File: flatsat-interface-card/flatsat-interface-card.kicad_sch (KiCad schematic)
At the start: 1 part, among them U1 MCP2221AxST

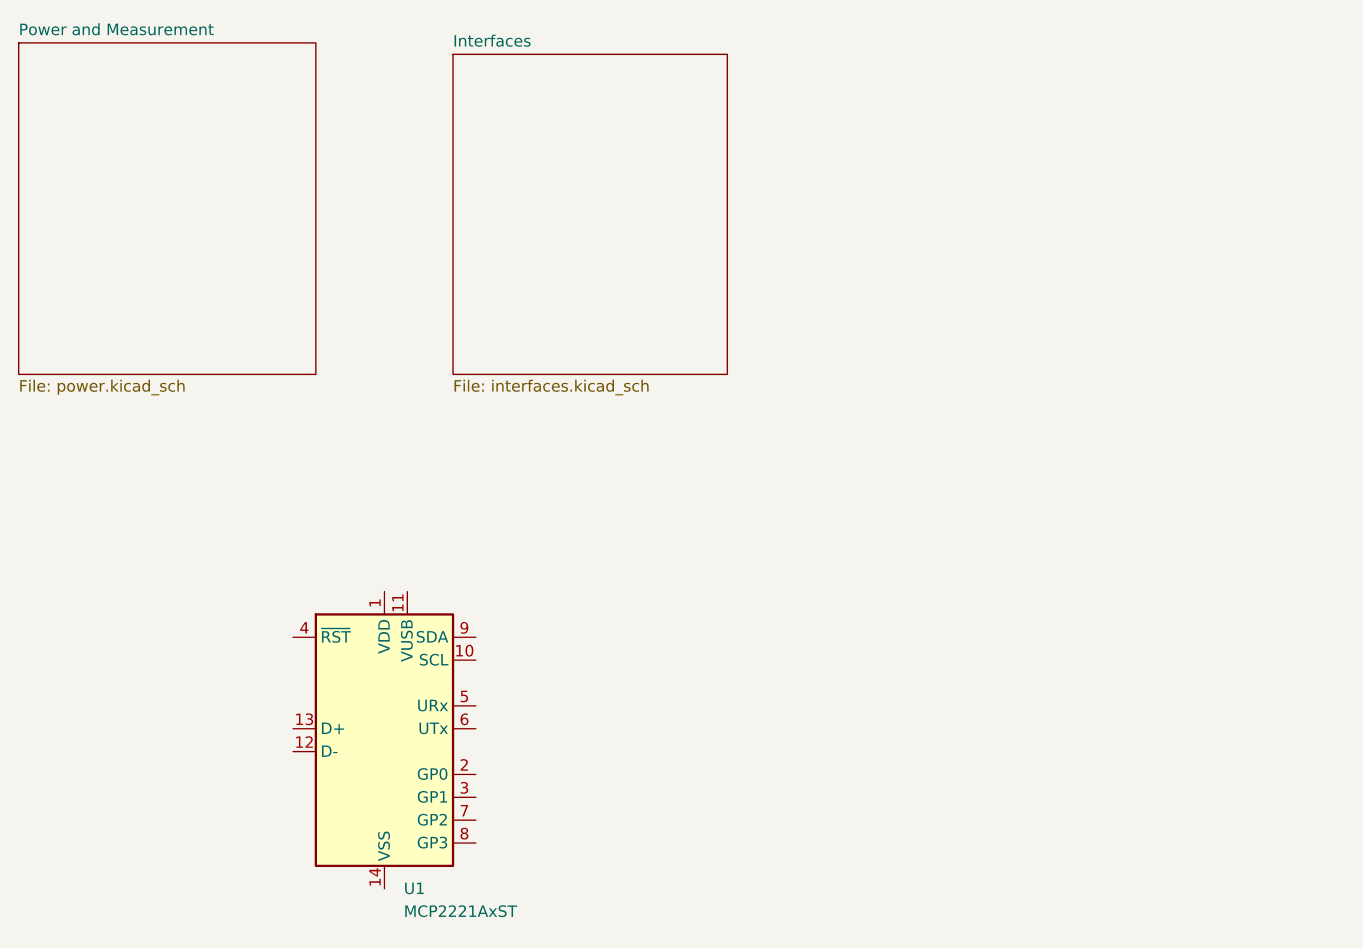
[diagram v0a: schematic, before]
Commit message: added new pages, identified i2c domain solution
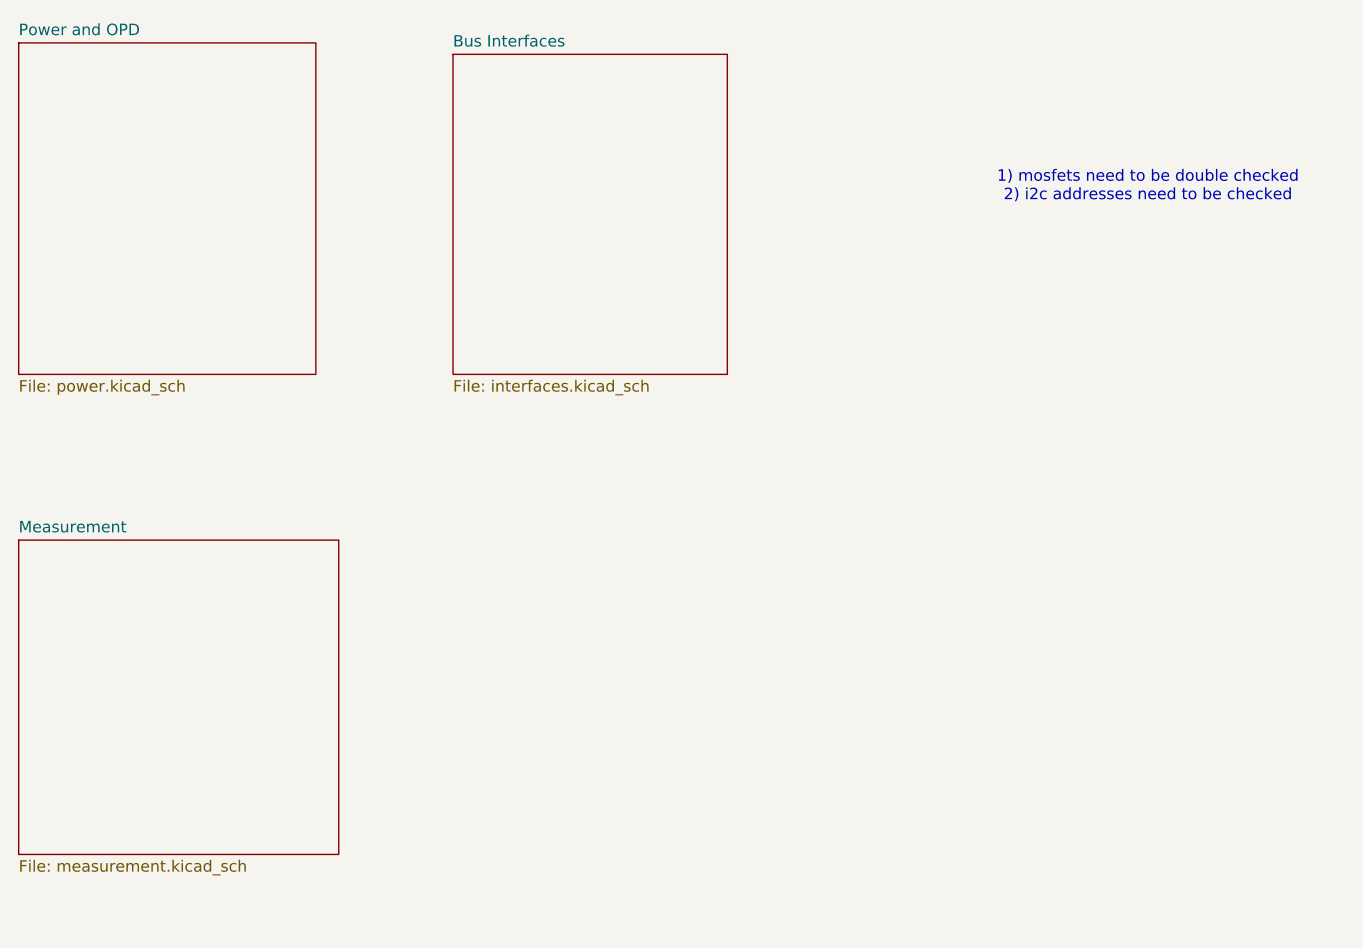
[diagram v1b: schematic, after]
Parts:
- removed U1: MCP2221AxST, Package_SO:TSSOP-14_4.4x5mm_P0.65mm, symbol Interface_USB:MCP2221AxST
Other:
- sheet Interfaces renamed Bus Interfaces
- sheet Power and Measurement renamed Power and OPD
- added sheet Measurement (measurement.kicad_sch)
- note added: "1) mosfets need to be double checked 2) i2c addresses need to be checked"
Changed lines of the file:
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@@
 	(title_block
 		(title "Flatsat Interface Card")
+		(date "2026-06-29")
 		(rev "0")
 		(company "Portland State Aerospace Society")
 	)
+	(text "1) mosfets need to be double checked\n2) i2c addresses need to be checked"
+		(exclude_from_sim no)
+		(at 221.996 54.102 0)
+		(effects
+			(font
+				(size 1.27 1.27)
+			)
+		)
+	)
 	(image
 		(at 257.81 173.99)
@@
 		)
 	)
-	(symbol
-		(lib_id "Interface_USB:MCP2221AxST")
-		(at 137.16 116.84 0)
-		(unit 1)
-		(body_style 1)
+	(sheet
+		(at 144.78 39.37)
+		(size 30.48 35.56)
 		(exclude_from_sim no)
 		(in_bom yes)
 		(on_board yes)
-		(in_pos_files yes)
 		(dnp no)
 		(fields_autoplaced yes)
-		(property "Reference" "U1"
-			(at 139.3033 132.08 0)
-			(show_name no)
-			(do_not_autoplace no)
-			(effects
-				(font
-					(size 1.27 1.27)
-				)
-				(justify left)
-			)
-		)
-		(property "Value" "MCP2221AxST"
-			(at 139.3033 134.62 0)
-			(show_name no)
-			(do_not_autoplace no)
-			(effects
-				(font
-					(size 1.27 1.27)
-				)
-				(justify left)
-			)
+		(stroke
+			(width 0.1524)
+			(type solid)
 		)
-		(property "Footprint" "Package_SO:TSSOP-14_4.4x5mm_P0.65mm"
-			(at 137.16 91.44 0)
-			(hide yes)
-			(show_name no)
-			(do_not_autoplace no)
-			(effects
-				(font
-					(size 1.27 1.27)
-				)
-			)
+		(fill
+			(color 0 0 0 0)
 		)
-		(property "Datasheet" "http://ww1.microchip.com/downloads/en/DeviceDoc/20005565B.pdf"
-			(at 137.16 99.06 0)
-			(hide yes)
+		(property "Sheetname" "Bus Interfaces"
+			(at 144.78 38.6584 0)
 			(show_name no)
 			(do_not_autoplace no)
@@
 					(size 1.27 1.27)
 				)
+				(justify left bottom)
 			)
 		)
-		(property "Description" "USB to I2C/UART Protocol Converter with GPIO, TSSOP-14"
-			(at 137.16 116.84 0)
-			(hide yes)
+		(property "Sheetfile" "interfaces.kicad_sch"
+			(at 144.78 75.5146 0)
 			(show_name no)
 			(do_not_autoplace no)
@@
 					(size 1.27 1.27)
 				)
+				(justify left top)
 			)
 		)
-		(pin "6"
-		)
-		(pin "2"
-		)
-		(pin "1"
-		)
-		(pin "4"
-		)
-		(pin "3"
-		)
-		(pin "5"
-		)
-		(pin "7"
-		)
-		(pin "11"
-		)
-		(pin "10"
-		)
-		(pin "9"
-		)
-		(pin "8"
-		)
-		(pin "14"
-		)
-		(pin "13"
-		)
-		(pin "12"
-		)
 		(instances
 			(project "flatsat-interface-card"
 				(path "/1a9202c4-e698-4c93-952c-ee3e64e9e49c"
-					(reference "U1")
-					(unit 1)
+					(page "3")
 				)
 			)
@@
 	)
 	(sheet
-		(at 144.78 39.37)
-		(size 30.48 35.56)
+		(at 96.52 38.1)
+		(size 33.02 36.83)
 		(exclude_from_sim no)
 		(in_bom yes)
@@
 			(color 0 0 0 0)
 		)
-		(property "Sheetname" "Interfaces"
-			(at 144.78 38.6584 0)
+		(property "Sheetname" "Power and OPD"
+			(at 96.52 37.3884 0)
 			(show_name no)
 			(do_not_autoplace no)
@@
 			)
 		)
-		(property "Sheetfile" "interfaces.kicad_sch"
-			(at 144.78 75.5146 0)
+		(property "Sheetfile" "power.kicad_sch"
+			(at 96.52 75.5146 0)
 			(show_name no)
 			(do_not_autoplace no)
@@
 			)
 		)
+		(property "Field2" ""
+			(at 96.52 38.1 0)
+			(hide yes)
+			(show_name no)
+			(do_not_autoplace no)
+			(effects
+				(font
+					(size 1.27 1.27)
+				)
+			)
+		)
 		(instances
 			(project "flatsat-interface-card"
 				(path "/1a9202c4-e698-4c93-952c-ee3e64e9e49c"
-					(page "3")
+					(page "2")
 				)
 			)
@@
 	)
 	(sheet
-		(at 96.52 38.1)
-		(size 33.02 36.83)
+		(at 96.52 93.345)
+		(size 35.56 34.925)
 		(exclude_from_sim no)
 		(in_bom yes)
@@
 			(color 0 0 0 0)
 		)
-		(property "Sheetname" "Power and Measurement"
-			(at 96.52 37.3884 0)
+		(property "Sheetname" "Measurement"
+			(at 96.52 92.6334 0)
 			(show_name no)
 			(do_not_autoplace no)
@@
 			)
 		)
-		(property "Sheetfile" "power.kicad_sch"
-			(at 96.52 75.5146 0)
+		(property "Sheetfile" "measurement.kicad_sch"
+			(at 96.52 128.8546 0)
 			(show_name no)
 			(do_not_autoplace no)
@@
 		)
 		(property "Field2" ""
-			(at 96.52 38.1 0)
+			(at 96.52 93.345 0)
 			(hide yes)
 			(show_name no)
@@
 			(project "flatsat-interface-card"
 				(path "/1a9202c4-e698-4c93-952c-ee3e64e9e49c"
-					(page "2")
+					(page "4")
 				)
 			)

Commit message: cleaned up schematic more
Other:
- sheet Bus Interfaces ports: added backplane; removed none
- sheet Measurement ports: added USB+, USB-, USBShutdown, backplane; removed none
- sheet Power and OPD ports: added USB+, USB-, USBShutdown, backplane; removed none
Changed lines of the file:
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@@
 		)
 	)
+	(junction
+		(at 137.16 62.23)
+		(diameter 0)
+		(color 0 0 0 0)
+	)
+	(bus
+		(pts
+			(xy 129.54 62.23) (xy 137.16 62.23)
+		)
+		(stroke
+			(width 0)
+			(type default)
+		)
+	)
+	(bus
+		(pts
+			(xy 132.08 111.76) (xy 137.16 111.76)
+		)
+		(stroke
+			(width 0)
+			(type default)
+		)
+	)
+	(bus
+		(pts
+			(xy 137.16 62.23) (xy 144.78 62.23)
+		)
+		(stroke
+			(width 0)
+			(type default)
+		)
+	)
+	(wire
+		(pts
+			(xy 121.92 74.93) (xy 121.92 99.06)
+		)
+		(stroke
+			(width 0)
+			(type default)
+		)
+	)
+	(wire
+		(pts
+			(xy 119.38 74.93) (xy 119.38 99.06)
+		)
+		(stroke
+			(width 0)
+			(type default)
+		)
+	)
+	(bus
+		(pts
+			(xy 137.16 62.23) (xy 137.16 111.76)
+		)
+		(stroke
+			(width 0)
+			(type default)
+		)
+	)
+	(wire
+		(pts
+			(xy 106.68 74.93) (xy 106.68 99.06)
+		)
+		(stroke
+			(width 0)
+			(type default)
+		)
+	)
 	(image
 		(at 257.81 173.99)
@@
 			)
 		)
+		(pin "backplane" input
+			(at 144.78 62.23 180)
+			(effects
+				(font
+					(size 1.27 1.27)
+				)
+				(justify left)
+			)
+		)
 		(instances
 			(project "flatsat-interface-card"
@@
 			)
 		)
+		(pin "USB+" input
+			(at 121.92 74.93 270)
+			(effects
+				(font
+					(size 1.27 1.27)
+				)
+				(justify left)
+			)
+		)
+		(pin "USB-" input
+			(at 119.38 74.93 270)
+			(effects
+				(font
+					(size 1.27 1.27)
+				)
+				(justify left)
+			)
+		)
+		(pin "USBShutdown" input
+			(at 106.68 74.93 270)
+			(effects
+				(font
+					(size 1.27 1.27)
+				)
+				(justify left)
+			)
+		)
+		(pin "backplane" input
+			(at 129.54 62.23 0)
+			(effects
+				(font
+					(size 1.27 1.27)
+				)
+				(justify right)
+			)
+		)
 		(instances
 			(project "flatsat-interface-card"
@@
 	)
 	(sheet
-		(at 96.52 93.345)
+		(at 96.52 99.06)
 		(size 35.56 34.925)
 		(exclude_from_sim no)
@@
 		)
 		(property "Sheetname" "Measurement"
-			(at 96.52 92.6334 0)
+			(at 96.52 98.3484 0)
 			(show_name no)
 			(do_not_autoplace no)
@@
 		)
 		(property "Sheetfile" "measurement.kicad_sch"
-			(at 96.52 128.8546 0)
+			(at 96.52 134.5696 0)
 			(show_name no)
 			(do_not_autoplace no)
@@
 		)
 		(property "Field2" ""
-			(at 96.52 93.345 0)
+			(at 96.52 99.06 0)
 			(hide yes)
 			(show_name no)
@@
 			)
 		)
+		(pin "backplane" input
+			(at 132.08 111.76 0)
+			(effects
+				(font
+					(size 1.27 1.27)
+				)
+				(justify right)
+			)
+		)
+		(pin "USBShutdown" input
+			(at 106.68 99.06 90)
+			(effects
+				(font
+					(size 1.27 1.27)
+				)
+				(justify right)
+			)
+		)
+		(pin "USB-" input
+			(at 119.38 99.06 90)
+			(effects
+				(font
+					(size 1.27 1.27)
+				)
+				(justify right)
+			)
+		)
+		(pin "USB+" input
+			(at 121.92 99.06 90)
+			(effects
+				(font
+					(size 1.27 1.27)
+				)
+				(justify right)
+			)
+		)
